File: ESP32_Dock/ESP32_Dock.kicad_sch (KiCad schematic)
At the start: 7 parts, among them J1 Conn_01x04, J2 Conn_01x04, J3 Conn_01x04, J4 Conn_01x07, J5 Conn_01x13

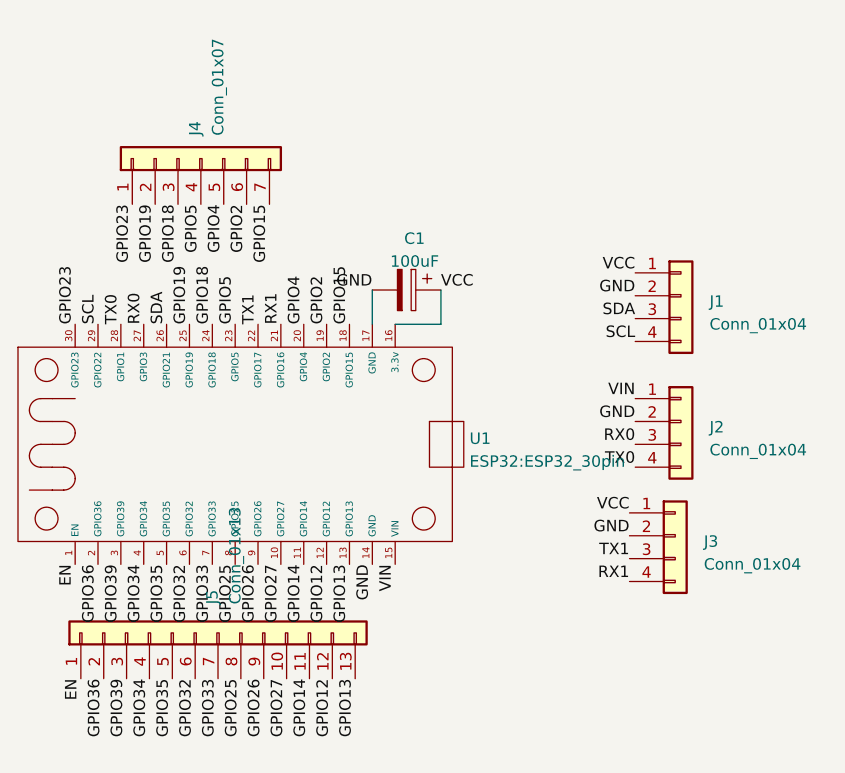
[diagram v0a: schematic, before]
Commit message: Fixed capacitor size on ESP32 dock
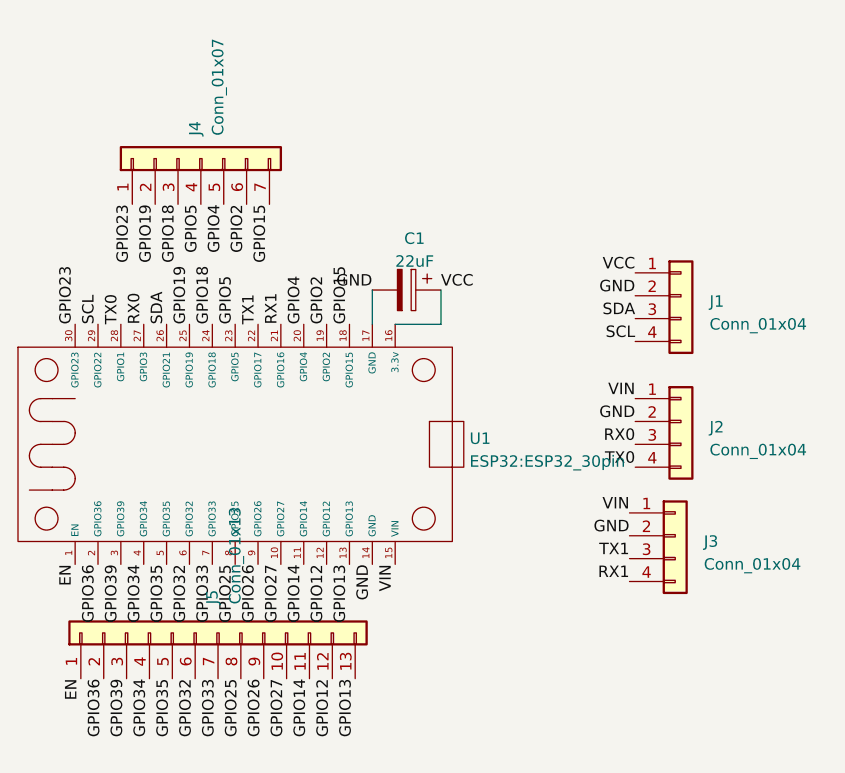
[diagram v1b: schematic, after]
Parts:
- C1: value 100uF -> 22uF; footprint Capacitor_THT:C_Radial_D4.0mm_H5.0mm_P1.50mm -> Capacitor_THT:C_Radial_D5.0mm_H11.0mm_P2.00mm
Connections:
- net VCC: no longer J3.1 (Pin_1)
- net VIN: now also J3.1 (Pin_1)
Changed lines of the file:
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@@
     (effects (font (size 1.27 1.27)) (justify left bottom))
   )
-  (label "VCC" (at 99.06 46.99 180) (fields_autoplaced)
+  (label "VIN" (at 99.06 46.99 180) (fields_autoplaced)
     (effects (font (size 1.27 1.27)) (justify right bottom))
   )
@@
       (effects (font (size 1.27 1.27)))
     )
-    (property "Value" "100uF" (at 75.184 19.05 90)
+    (property "Value" "22uF" (at 75.184 19.05 90)
       (effects (font (size 1.27 1.27)))
     )
-    (property "Footprint" "Capacitor_THT:C_Radial_D4.0mm_H5.0mm_P1.50mm" (at 70.485 23.1902 0)
+    (property "Footprint" "Capacitor_THT:C_Radial_D5.0mm_H11.0mm_P2.00mm" (at 70.485 23.1902 0)
       (effects (font (size 1.27 1.27)) hide)
     )
